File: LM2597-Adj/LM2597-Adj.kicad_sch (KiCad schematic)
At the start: 12 parts, among them IC1 LM2597MX-ADJ_NOPB, J1 Conn_01x05

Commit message: routed and drc'ed
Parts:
- removed C1, C3: 0.1uF, Capacitor_THT:C_Rect_L9.0mm_W3.6mm_P7.50mm_MKT, symbol Device:C
- removed C2: 3.3nF, Capacitor_THT:C_Rect_L9.0mm_W3.6mm_P7.50mm_MKT, symbol Device:C
- removed D1: 1N5817, SamacSys_Parts:DIOAD1414W86L464D238, symbol SamacSys_Parts:1N5817
- removed J1: Conn_01x05, Connector_PinHeader_2.54mm:PinHeader_1x05_P2.54mm_Vertical, symbol Connector_Generic:Conn_01x05
- added C3 (x3): 0.1uF, Capacitor_SMD:C_0603_1608Metric_Pad1.08x0.95mm_HandSolder, symbol Device:C
- added D1: 1N5817, Diode_THT:D_DO-41_SOD81_P10.16mm_Horizontal, symbol Diode:1N5817
- added J1: Conn_01x03, Connector_PinHeader_2.54mm:PinHeader_1x03_P2.54mm_Vertical, symbol Connector_Generic:Conn_01x03
- R2, R3: footprint Resistor_THT:R_Axial_DIN0204_L3.6mm_D1.6mm_P7.62mm_Horizontal -> Resistor_THT:R_Axial_DIN0207_L6.3mm_D2.5mm_P2.54mm_Vertical
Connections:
- net +12V is gone; now on net +VDC: C4.1, IC1.7 (+VIN)
- net +VDC: now also R1.2, J1.1 (Pin_1)
- net GND: now also C3.2, C3.2, D1.2 (A), J1.3 (Pin_3)
- net at IC1.2 (DELAY): now also C3.1
- net at IC1.4 (FEEDBACK), R2.1, R3.2: now also C3.1
- net at IC1.5 (~{SHUTDOWN}/SOFT-START): now also C3.1
- net at IC1.8 (OUTPUT), L1.1: now also D1.1 (K)
- net +9V renamed VCC
- net VCC: now also C3.2, J1.2 (Pin_2); no longer R1.2

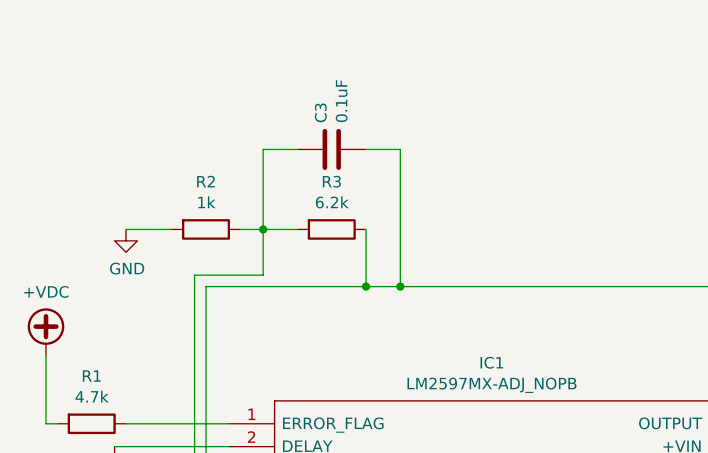
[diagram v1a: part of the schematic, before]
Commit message: updated all of these to SMD parts
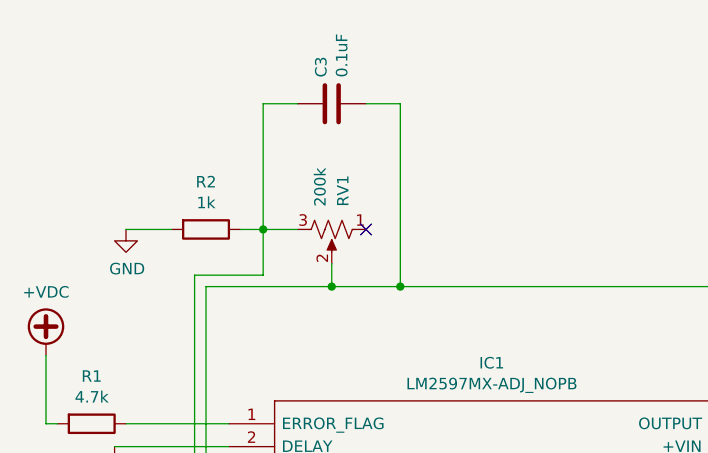
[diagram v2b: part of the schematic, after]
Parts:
- removed R3: 6.2k, Resistor_THT:R_Axial_DIN0207_L6.3mm_D2.5mm_P2.54mm_Vertical, symbol Device:R
- added RV1: 200k, Potentiometer_THT:Potentiometer_Bourns_3296W_Vertical, symbol Device:R_Potentiometer_US
- C3: footprint Capacitor_SMD:C_0603_1608Metric_Pad1.08x0.95mm_HandSolder -> Capacitor_SMD:C_1206_3216Metric_Pad1.33x1.80mm_HandSolder
- R1, R2: footprint Resistor_THT:R_Axial_DIN0207_L6.3mm_D2.5mm_P2.54mm_Vertical -> Resistor_SMD:R_1206_3216Metric_Pad1.30x1.75mm_HandSolder
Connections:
- net VCC: now also RV1.2
- net at C3.1, IC1.4 (FEEDBACK), R2.1: now also RV1.3
- no-connect marks 0 -> 1
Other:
- moved on the sheet: C3
